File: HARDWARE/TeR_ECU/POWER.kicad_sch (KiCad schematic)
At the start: 13 parts, among them U2 TSR_1-2450, U3 LM1117MP-3.3, U4 TSR_1-24120

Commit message: Empezado el Layout
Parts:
- L1: footprint Footprints:IND_TCK-141_TRP -> footprints:IND_TCK-141_TRP
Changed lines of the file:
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@@
       (project "TeR_ECU"
         (path "/84413845-c4f3-4743-bcd2-a67649c90902/b76a95f3-584c-4daf-bbe9-70945b593e94"
-          (reference "#PWR017") (unit 1)
+          (reference "#PWR0106") (unit 1)
         )
       )
@@
       (project "TeR_ECU"
         (path "/84413845-c4f3-4743-bcd2-a67649c90902/b76a95f3-584c-4daf-bbe9-70945b593e94"
-          (reference "#PWR012") (unit 1)
+          (reference "#PWR0104") (unit 1)
         )
       )
@@
       (project "TeR_ECU"
         (path "/84413845-c4f3-4743-bcd2-a67649c90902/b76a95f3-584c-4daf-bbe9-70945b593e94"
-          (reference "C16") (unit 1)
+          (reference "C22") (unit 1)
         )
       )
@@
       (effects (font (size 1.524 1.524)))
     )
-    (property "Footprint" "Footprints:IND_TCK-141_TRP" (at 44.45 83.82 0)
+    (property "Footprint" "footprints:IND_TCK-141_TRP" (at 44.45 83.82 0)
       (effects (font (size 1.27 1.27) italic) hide)
     )
@@
       (project "TeR_ECU"
         (path "/84413845-c4f3-4743-bcd2-a67649c90902/b76a95f3-584c-4daf-bbe9-70945b593e94"
-          (reference "#PWR019") (unit 1)
+          (reference "#PWR0105") (unit 1)
         )
       )
@@
       (project "TeR_ECU"
         (path "/84413845-c4f3-4743-bcd2-a67649c90902/b76a95f3-584c-4daf-bbe9-70945b593e94"
-          (reference "#PWR011") (unit 1)
+          (reference "#PWR0103") (unit 1)
         )
       )
@@
       (project "TeR_ECU"
         (path "/84413845-c4f3-4743-bcd2-a67649c90902/b76a95f3-584c-4daf-bbe9-70945b593e94"
-          (reference "#PWR010") (unit 1)
+          (reference "#PWR0101") (unit 1)
         )
       )
@@
       (effects (font (size 1.524 1.524)))
     )
-    (property "Footprint" "Footprints:IND_TCK-141_TRP" (at 48.26 34.29 0)
+    (property "Footprint" "footprints:IND_TCK-141_TRP" (at 48.26 34.29 0)
       (effects (font (size 1.27 1.27) italic) hide)
     )
@@
       (project "TeR_ECU"
         (path "/84413845-c4f3-4743-bcd2-a67649c90902/b76a95f3-584c-4daf-bbe9-70945b593e94"
-          (reference "#PWR013") (unit 1)
-        )
-      )
+          (reference "#PWR0102") (unit 1)
+        )
+      )

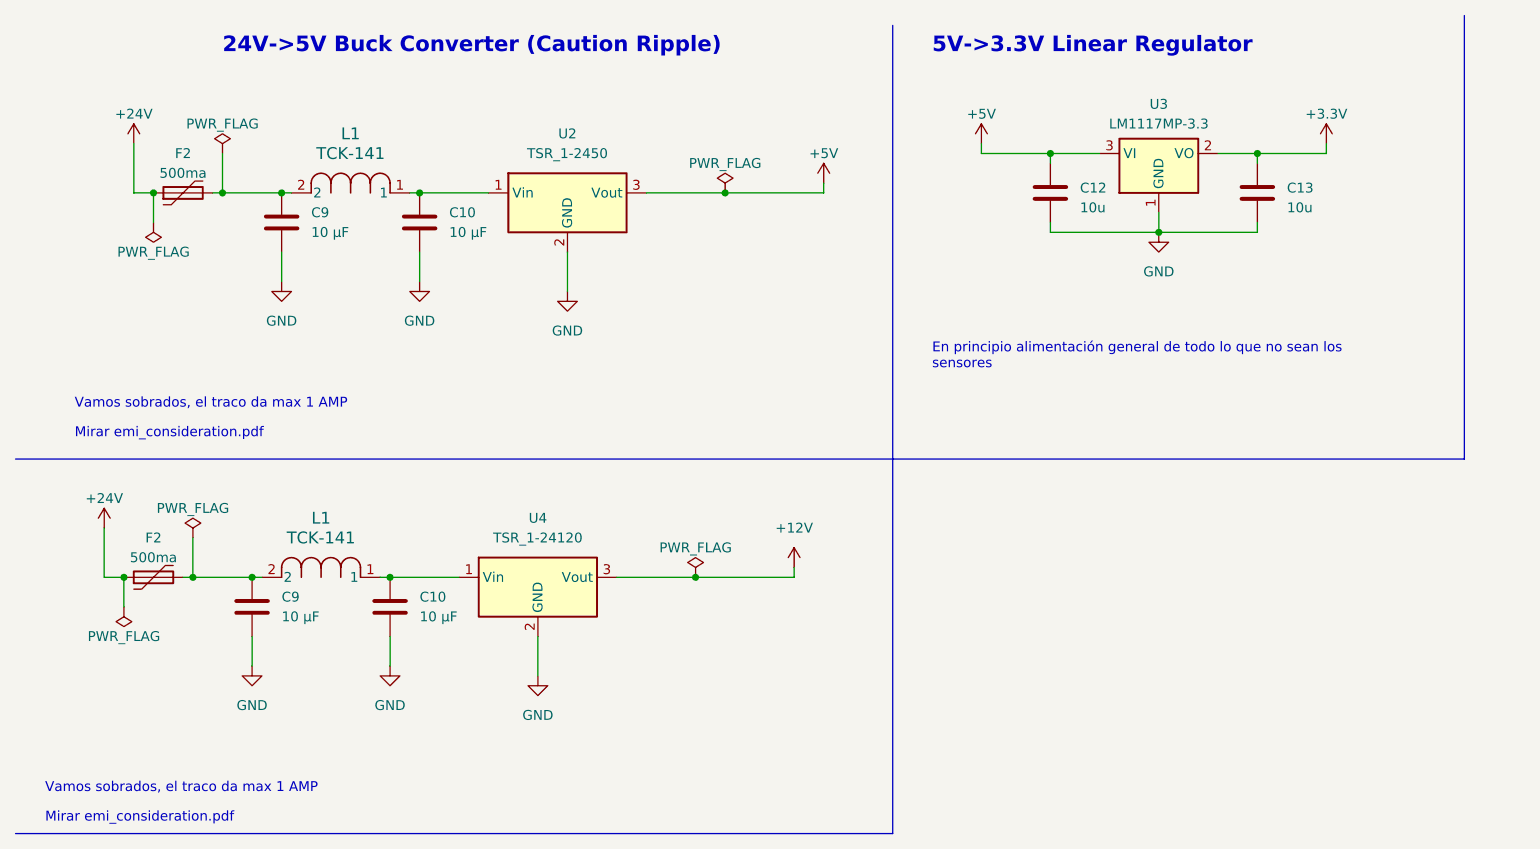
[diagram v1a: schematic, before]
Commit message: Rethought layout and footprints and fixed fuse normative problem
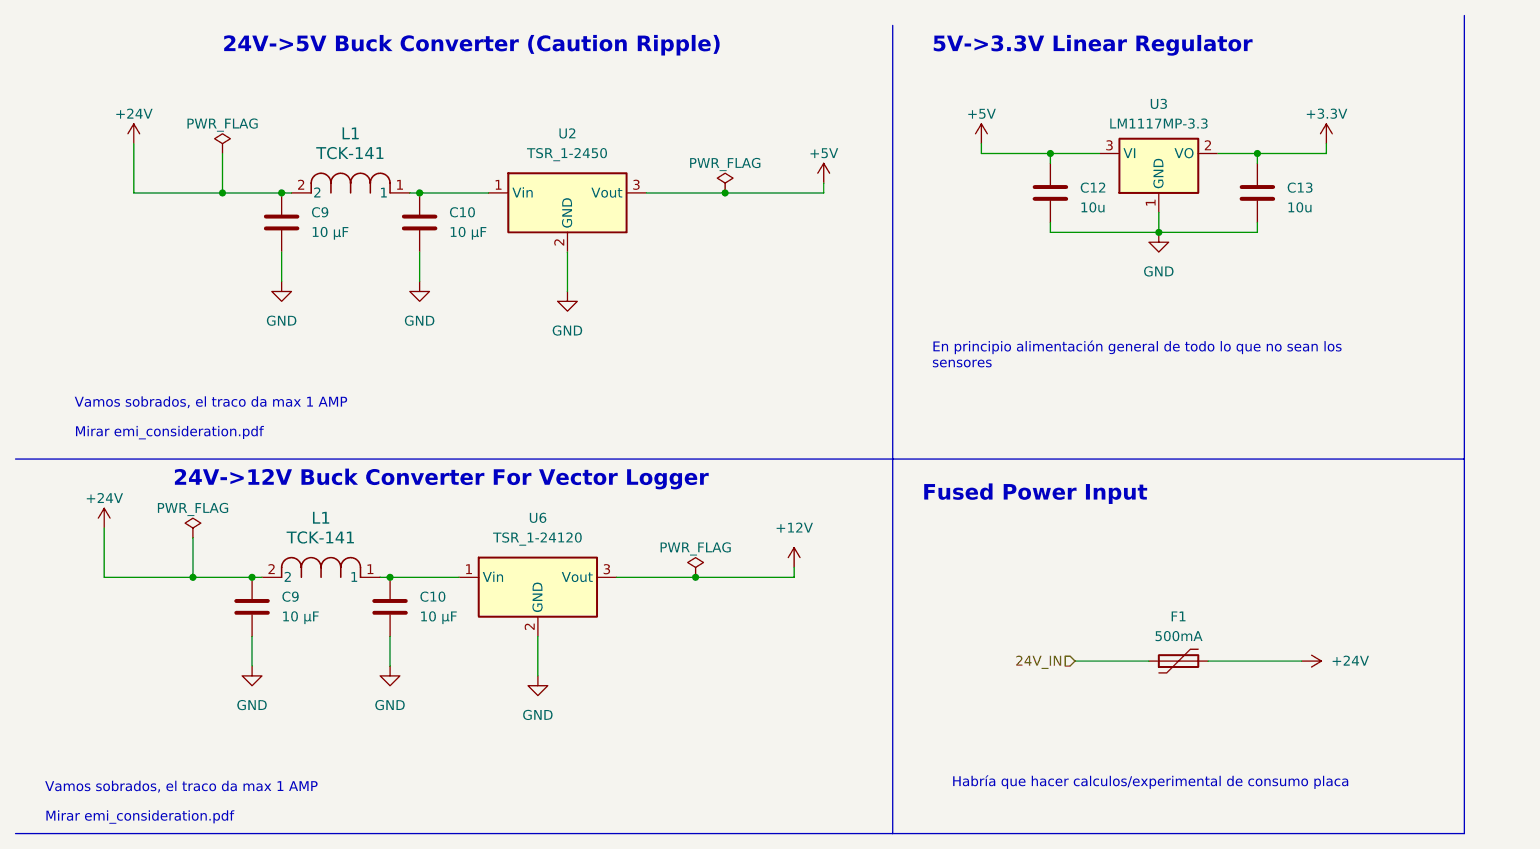
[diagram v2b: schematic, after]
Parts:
- removed F2 (x2): 500ma, Fuse:Fuse_0805_2012Metric, symbol Device:Polyfuse
- added F1: 500mA, symbol Device:Polyfuse
- renumbered U4 to U6
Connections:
- net +24V: now also C9.1, C9.1, L1.2, L1.2, F1.2
- new net 24V_IN: F1.1
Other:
- note added: "24V->12V Buck Converter For Vector Logger"
- note added: "Fused Power Input"
- note added: "Habría que hacer calculos/experimental de consumo placa"

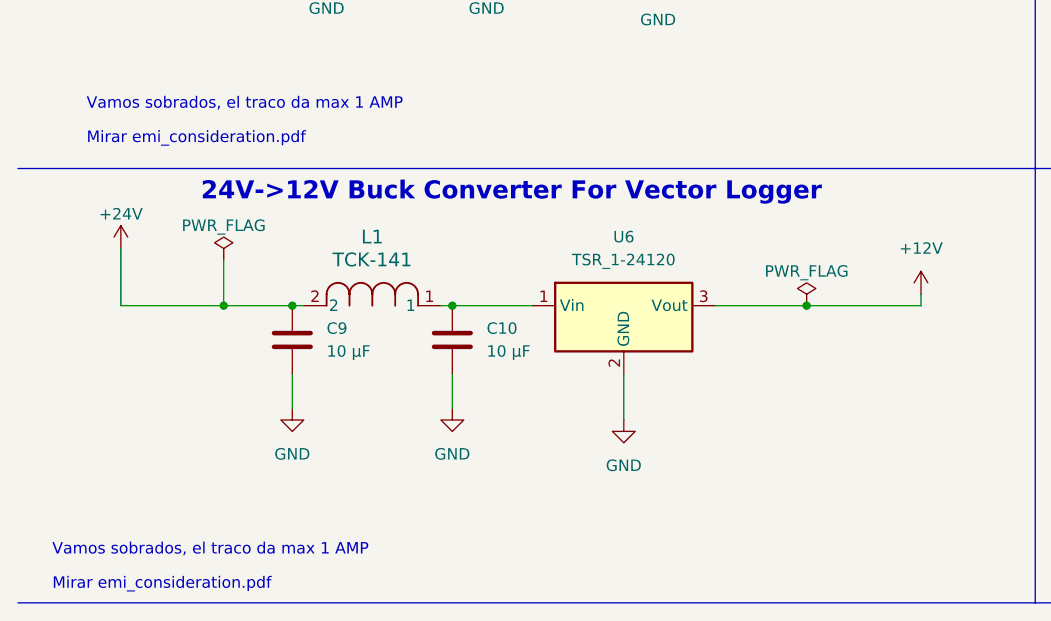
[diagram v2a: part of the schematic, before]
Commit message: Rethought layout and added pulldown to Horn mosfet
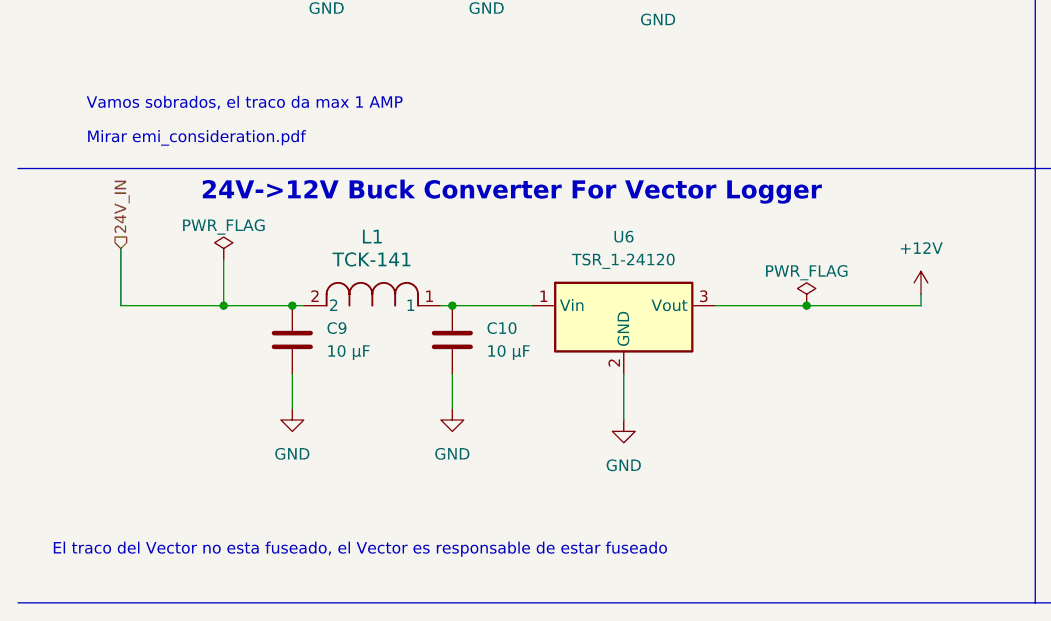
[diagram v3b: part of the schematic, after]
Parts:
- F1: footprint (none) -> Fuse:Fuse_0805_2012Metric
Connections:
- net +24V: no longer C9.1, L1.2
- net 24V_IN: now also C9.1, L1.2
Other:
- note added: "El traco del Vector no esta fuseado, el Vector es responsable de estar fuseado"
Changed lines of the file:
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@@
     (stroke (width 0) (type default))
   )
-  (text "Vamos sobrados, el traco da max 1 AMP" (at 16.51 111.76 0)
+  (text "El traco del Vector no esta fuseado, el Vector es responsable de estar fuseado\n"
+    (at 16.51 111.76 0)
     (effects (font (size 1.27 1.27)) (justify left bottom))
   )
@@
     (effects (font (size 1.27 1.27)) (justify left bottom))
   )
-  (text "Mirar emi_consideration.pdf\n" (at 16.51 115.57 0)
-    (effects (font (size 1.27 1.27)) (justify left bottom))
-  )
   (text "24V->12V Buck Converter For Vector Logger" (at 33.02 72.39 0)
     (effects (font (size 2 2) (thickness 0.4) bold) (justify left bottom))
@@
   (hierarchical_label "24V_IN" (shape input) (at 149.225 94.615 180) (fields_autoplaced)
     (effects (font (size 1.27 1.27)) (justify right))
+  )
+  (hierarchical_label "24V_IN" (shape input) (at 24.13 77.47 90) (fields_autoplaced)
+    (effects (font (size 1.27 1.27)) (justify left))
   )
   (symbol (lib_id "power:GND") (at 160.02 39.37 0) (unit 1)
@@
       (effects (font (size 1.27 1.27)))
     )
-    (property "Footprint" "" (at 167.64 93.345 0)
+    (property "Footprint" "Fuse:Fuse_0805_2012Metric" (at 167.64 93.345 0)
       (effects (font (size 1.27 1.27)) (justify left) hide)
     )
@@
         )
       )
-    )
-  )
-  (symbol (lib_id "power:+24V") (at 24.13 77.47 0) (unit 1)
-    (in_bom yes) (on_board yes) (dnp no) (fields_autoplaced)
-    (property "Reference" "#PWR010" (at 24.13 81.28 0)
-      (effects (font (size 1.27 1.27)) hide)
-    )
-    (property "Value" "+24V" (at 24.13 73.66 0)
-      (effects (font (size 1.27 1.27)))
-    )
-    (property "Footprint" "" (at 24.13 77.47 0)
-      (effects (font (size 1.27 1.27)) hide)
-    )
-    (property "Datasheet" "" (at 24.13 77.47 0)
-      (effects (font (size 1.27 1.27)) hide)
-    )
-    (pin "1")
-    (instances
-      (project "TER_PEDAL"
-        (path "/73ede3a3-6344-40fe-9207-10ff50d388ba/6f10bd65-583f-4818-aeb8-8b5e6e37f336"
-          (reference "#PWR010") (unit 1)
-        )
-      )
-      (project "TeR_ECU"
-        (path "/84413845-c4f3-4743-bcd2-a67649c90902/b76a95f3-584c-4daf-bbe9-70945b593e94"
-          (reference "#PWR047") (unit 1)
-        )
-      )

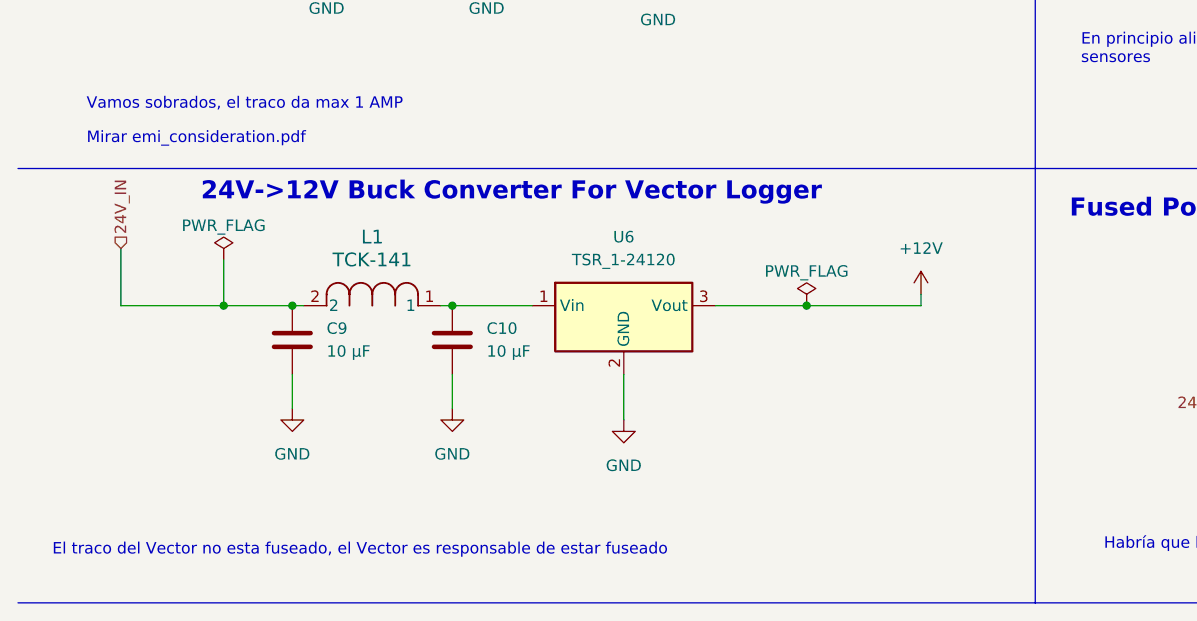
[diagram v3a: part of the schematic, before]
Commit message: Rethought project using an STM32NucleoF7
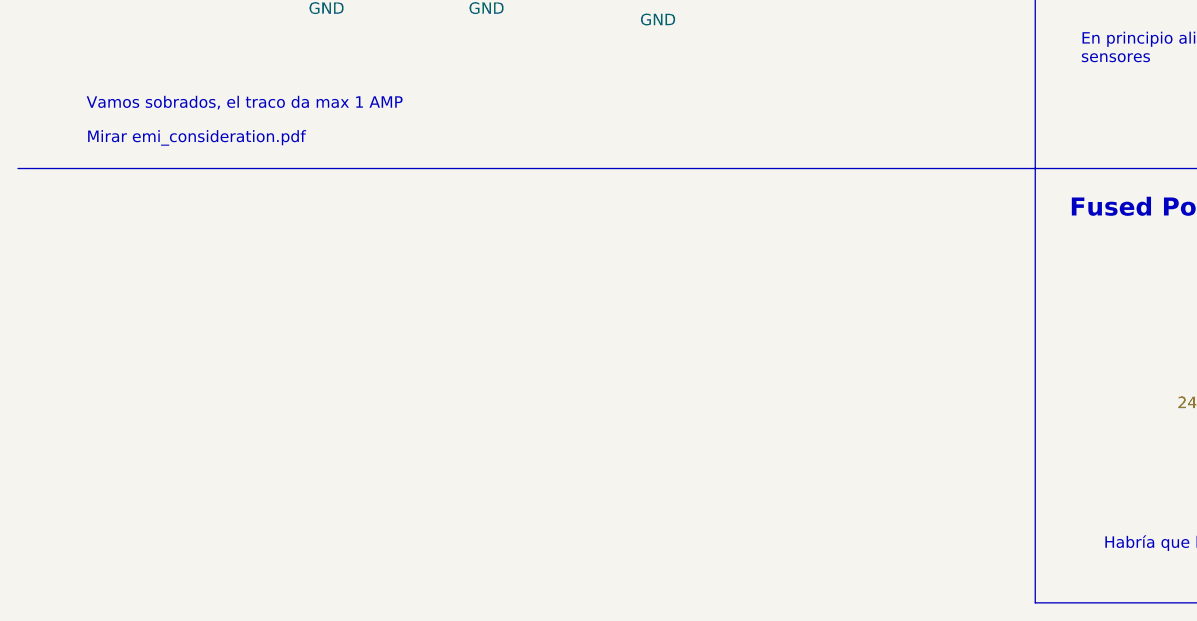
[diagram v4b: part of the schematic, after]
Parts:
- removed C10, C9: 10 µF, Capacitor_SMD:C_0805_2012Metric, symbol Device:C
- removed L1: TCK-141, footprints:IND_TCK-141_TRP, symbol TracoChoke:TCK-141
- removed U6: TSR_1-24120, Converter_DCDC:Converter_DCDC_TRACO_TSR-1_THT, symbol Regulator_Switching:TSR_1-24120
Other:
- note removed: "24V->12V Buck Converter For Vector Logger"
- note removed: "El traco del Vector no esta fuseado, el Vector es responsable de estar fuseado"

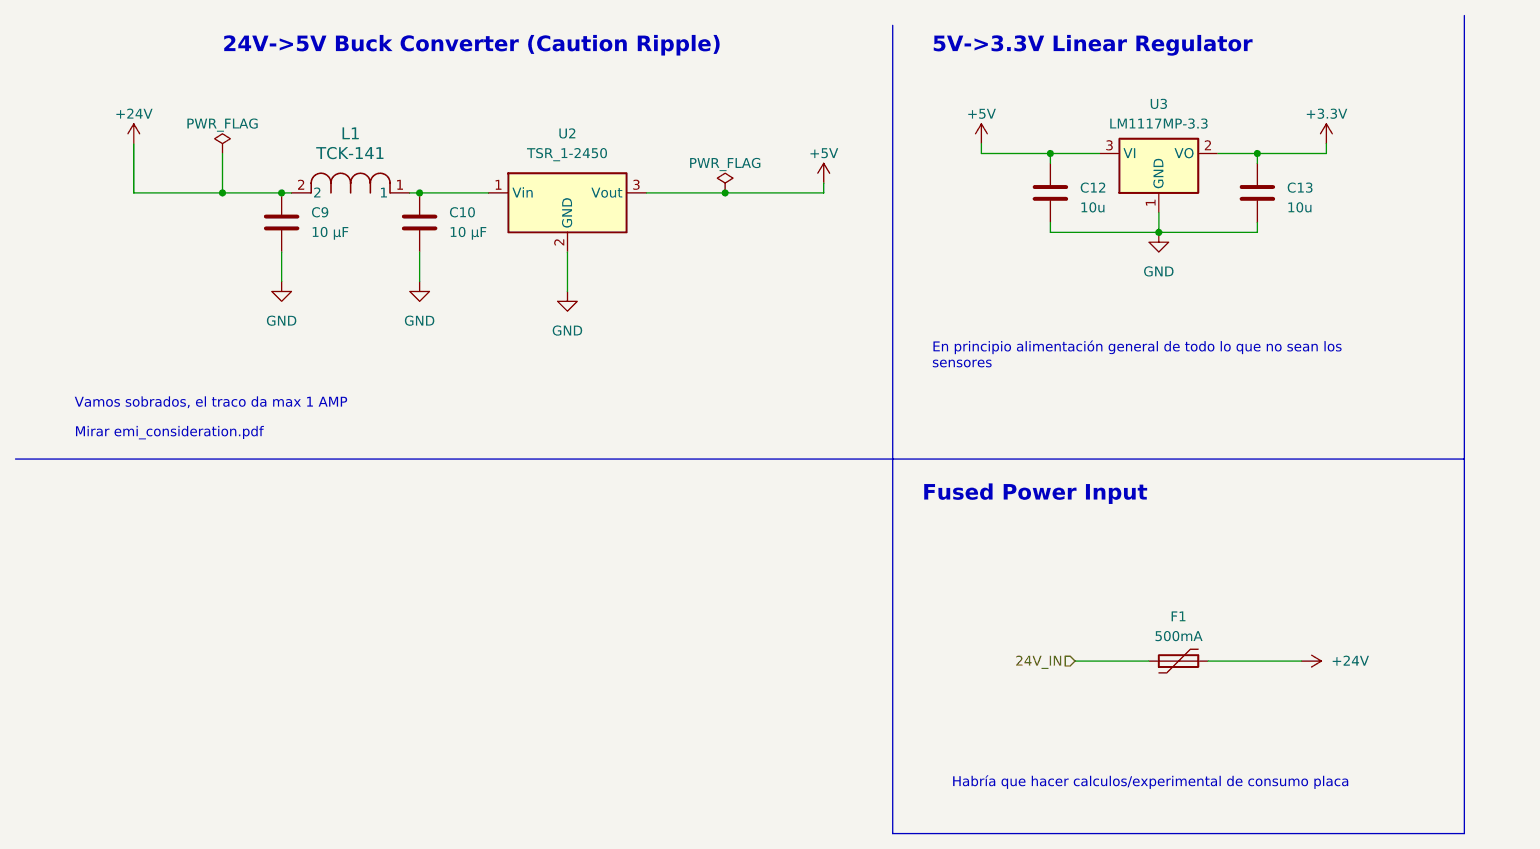
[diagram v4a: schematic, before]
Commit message: Finished re layout and adaption between the two versions
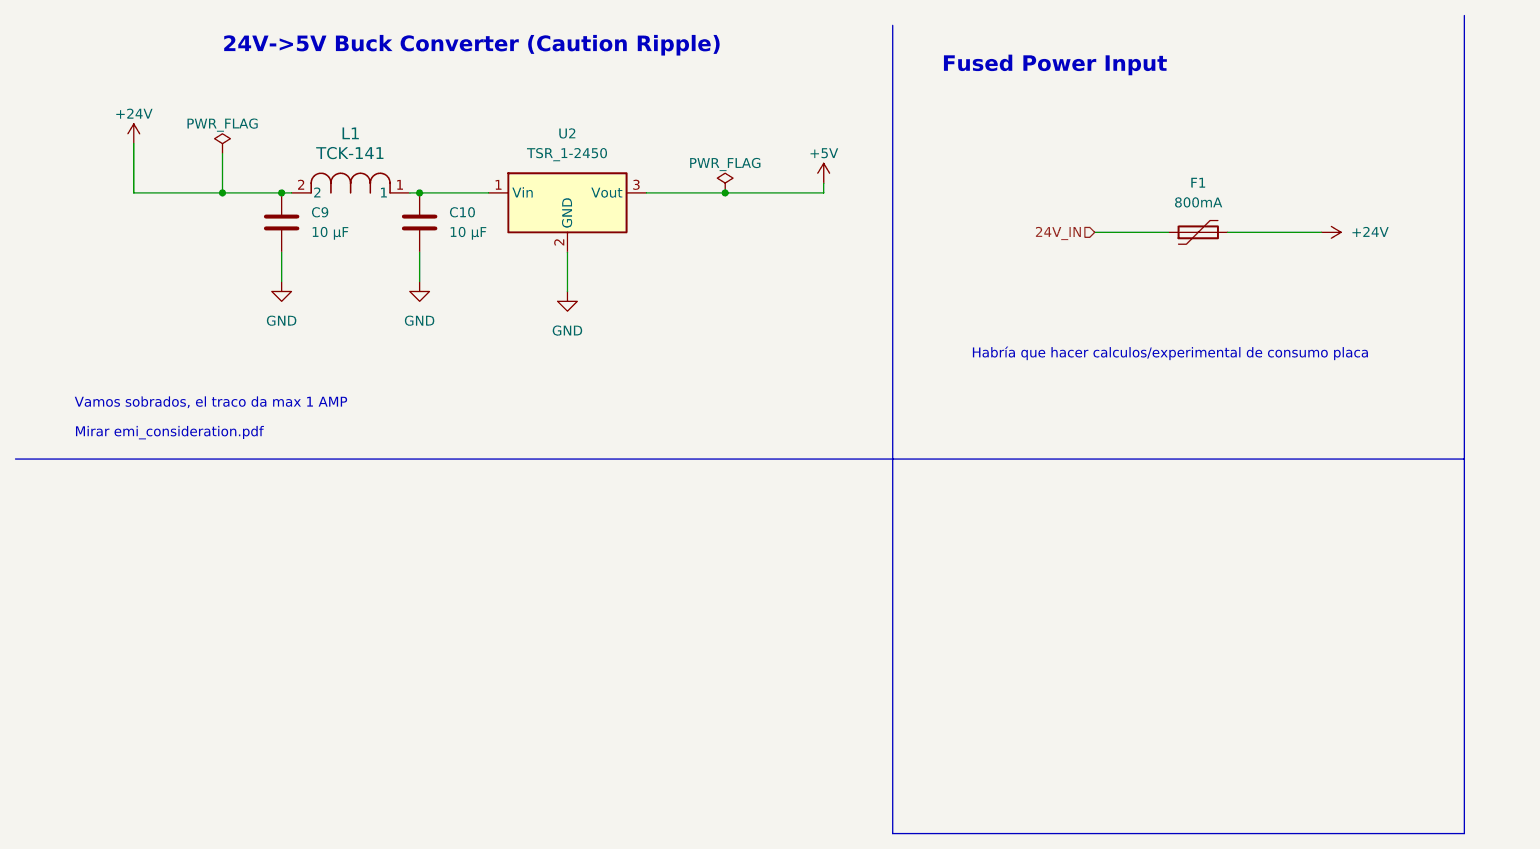
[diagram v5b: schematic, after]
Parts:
- removed C12, C13: 10u, Capacitor_SMD:C_0603_1608Metric, symbol Device:C
- removed U3: LM1117MP-3.3, Package_TO_SOT_SMD:SOT-223-3_TabPin2, symbol Regulator_Linear:LM1117MP-3.3
- F1: value 500mA -> 800mA
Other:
- note removed: "5V->3.3V Linear Regulator"
- note removed: "En principio alimentación general de todo lo que no sean los sensores"
- moved on the sheet: F1
